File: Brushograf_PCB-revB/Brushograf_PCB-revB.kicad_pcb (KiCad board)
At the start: 2 copper layers, 200 x 75 mm, 75 parts, among them J1 Conn_01x05_Socket, J12 USB-C PD in, J13 Pendant, J2 Conn_01x05_Socket, J3 Conn_01x05_Socket, J8 SD_CARD_MICRO_AMPHENOL_114008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, SW1 ESP POWER, SW2 SW_Lever_1P2T_NKK_GW12LxH, U1 ULN2003A, U2 ULN2003A, U3 ULN2003A, U4 ESP32-DevKitC, U6 CH224K, U7 TPS54202, U8 TPS54202

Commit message: Rotate piezo pickup headers to be horizontal and mathematically center them
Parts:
- moved J_X_Pickup 3.81 mm to (126.2, 38.0), turned to 90 degrees
- moved J_Y_Pickup 3.81 mm to (186.2, 38.0), turned to 90 degrees
- moved J_Z_Pickup 3.81 mm to (66.2, 38.0), turned to 90 degrees
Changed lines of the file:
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@@
 		(locked yes)
 		(layer "F.Cu")
-		(at 130 38)
+		(at 126.19 38 90)
 		(descr "Through hole straight pin header, 1x04, 2.54mm pitch, single row")
 		(tags "Through hole pin header THT 1x04 2.54mm single row")
 		(property "Reference" "J_X_Pickup"
-			(at 0 -2.38 0)
+			(at 0 -2.38 90)
 			(layer "F.SilkS")
 			(effects
@@
 		)
 		(property "Value" "PinHeader_1x04_P2.54mm_Vertical"
-			(at 0 10 0)
+			(at 0 10 90)
 			(layer "F.Fab")
 			(effects
@@
 		)
 		(property "Datasheet" ""
-			(at 0 0 0)
+			(at 0 0 90)
 			(layer "F.Fab")
 			(hide yes)
@@
 		)
 		(property "Description" ""
-			(at 0 0 0)
+			(at 0 0 90)
 			(layer "F.Fab")
 			(hide yes)
@@
 		)
 		(property "KiLib_Generator" "connector/pin_header_socket"
-			(at 0 0 0)
+			(at 0 0 90)
 			(layer "F.SilkS")
 			(hide yes)
@@
 		)
 		(fp_line
-			(start -1.38 1.27)
-			(end -1.38 9)
+			(start 1.38 1.27)
+			(end 1.38 9)
 			(stroke
 				(width 0.12)
@@
 		)
 		(fp_line
-			(start -1.38 9)
-			(end 1.38 9)
+			(start -1.38 1.27)
+			(end -1.38 9)
 			(stroke
 				(width 0.12)
@@
 		)
 		(fp_line
-			(start 1.38 1.27)
+			(start -1.38 9)
 			(end 1.38 9)
 			(stroke
@@
 		)
 		(fp_line
-			(start -1.27 -0.635)
-			(end -0.635 -1.27)
+			(start 1.27 -1.27)
+			(end 1.27 8.89)
 			(stroke
 				(width 0.1)
@@
 		)
 		(fp_line
-			(start -1.27 8.89)
-			(end -1.27 -0.635)
+			(start -0.635 -1.27)
+			(end 1.27 -1.27)
 			(stroke
 				(width 0.1)
@@
 		)
 		(fp_line
-			(start -0.635 -1.27)
-			(end 1.27 -1.27)
+			(start -1.27 -0.635)
+			(end -0.635 -1.27)
 			(stroke
 				(width 0.1)
@@
 		)
 		(fp_line
-			(start 1.27 -1.27)
-			(end 1.27 8.89)
+			(start 1.27 8.89)
+			(end -1.27 8.89)
 			(stroke
 				(width 0.1)
@@
 		)
 		(fp_line
-			(start 1.27 8.89)
-			(end -1.27 8.89)
+			(start -1.27 8.89)
+			(end -1.27 -0.635)
 			(stroke
 				(width 0.1)
@@
 		)
 		(fp_text user "${REFERENCE}"
-			(at 0 3.81 90)
+			(at 0 3.81 180)
 			(layer "F.Fab")
 			(effects
@@
 		)
 		(pad "1" thru_hole rect
-			(at 0 0)
+			(at 0 0 90)
 			(size 1.7 1.7)
 			(drill 1)
@@
 		)
 		(pad "2" thru_hole circle
-			(at 0 2.54)
+			(at 0 2.54 90)
 			(size 1.7 1.7)
 			(drill 1)
@@
 		)
 		(pad "3" thru_hole circle
-			(at 0 5.08)
+			(at 0 5.08 90)
 			(size 1.7 1.7)
 			(drill 1)
@@
 		)
 		(pad "4" thru_hole circle
-			(at 0 7.62)
+			(at 0 7.62 90)
 			(size 1.7 1.7)
 			(drill 1)
@@
 		(locked yes)
 		(layer "F.Cu")
-		(at 190 38)
+		(at 186.19 38 90)
 		(descr "Through hole straight pin header, 1x04, 2.54mm pitch, single row")
 		(tags "Through hole pin header THT 1x04 2.54mm single row")
 		(property "Reference" "J_Y_Pickup"
-			(at 0 -2.38 0)
+			(at 0 -2.38 90)
 			(layer "F.SilkS")
 			(effects
@@
 		)
 		(property "Value" "PinHeader_1x04_P2.54mm_Vertical"
-			(at 0 10 0)
+			(at 0 10 90)
 			(layer "F.Fab")
 			(effects
@@
 		)
 		(property "Datasheet" ""
-			(at 0 0 0)
+			(at 0 0 90)
 			(layer "F.Fab")
 			(hide yes)
@@
 		)
 		(property "Description" ""
-			(at 0 0 0)
+			(at 0 0 90)
 			(layer "F.Fab")
 			(hide yes)
@@
 		)
 		(property "KiLib_Generator" "connector/pin_header_socket"
-			(at 0 0 0)
+			(at 0 0 90)
 			(layer "F.SilkS")
 			(hide yes)
@@
 		)
 		(fp_line
-			(start -1.38 1.27)
-			(end -1.38 9)
+			(start 1.38 1.27)
+			(end 1.38 9)
 			(stroke
 				(width 0.12)
@@
 		)
 		(fp_line
-			(start -1.38 9)
-			(end 1.38 9)
+			(start -1.38 1.27)
+			(end -1.38 9)
 			(stroke
 				(width 0.12)
@@
 		)
 		(fp_line
-			(start 1.38 1.27)
+			(start -1.38 9)
 			(end 1.38 9)
 			(stroke
@@
 		)
 		(fp_line
-			(start -1.27 -0.635)
-			(end -0.635 -1.27)
+			(start 1.27 -1.27)
+			(end 1.27 8.89)
 			(stroke
 				(width 0.1)
@@
 		)
 		(fp_line
-			(start -1.27 8.89)
-			(end -1.27 -0.635)
+			(start -0.635 -1.27)
+			(end 1.27 -1.27)
 			(stroke
 				(width 0.1)
@@
 		)
 		(fp_line
-			(start -0.635 -1.27)
-			(end 1.27 -1.27)
+			(start -1.27 -0.635)
+			(end -0.635 -1.27)
 			(stroke
 				(width 0.1)
@@
 		)
 		(fp_line
-			(start 1.27 -1.27)
-			(end 1.27 8.89)
+			(start 1.27 8.89)
+			(end -1.27 8.89)
 			(stroke
 				(width 0.1)
@@
 		)
 		(fp_line
-			(start 1.27 8.89)
-			(end -1.27 8.89)
+			(start -1.27 8.89)
+			(end -1.27 -0.635)
 			(stroke
 				(width 0.1)
@@
 		)
 		(fp_text user "${REFERENCE}"
-			(at 0 3.81 90)
+			(at 0 3.81 180)
 			(layer "F.Fab")
 			(effects
@@
 		)
 		(pad "1" thru_hole rect
-			(at 0 0)
+			(at 0 0 90)
 			(size 1.7 1.7)
 			(drill 1)
@@
 		)
 		(pad "2" thru_hole circle
-			(at 0 2.54)
+			(at 0 2.54 90)
 			(size 1.7 1.7)
 			(drill 1)
@@
 		)
 		(pad "3" thru_hole circle
-			(at 0 5.08)
+			(at 0 5.08 90)
 			(size 1.7 1.7)
 			(drill 1)
@@
 		)
 		(pad "4" thru_hole circle
-			(at 0 7.62)
+			(at 0 7.62 90)
 			(size 1.7 1.7)
 			(drill 1)
@@
 		(locked yes)
 		(layer "F.Cu")
-		(at 70 38)
+		(at 66.19 38 90)
 		(descr "Through hole straight pin header, 1x04, 2.54mm pitch, single row")
 		(tags "Through hole pin header THT 1x04 2.54mm single row")
 		(property "Reference" "J_Z_Pickup"
-			(at 0 -2.38 0)
+			(at 0 -2.38 90)
 			(layer "F.SilkS")
 			(effects
@@
 		)
 		(property "Value" "PinHeader_1x04_P2.54mm_Vertical"
-			(at 0 10 0)
+			(at 0 10 90)
 			(layer "F.Fab")
 			(effects
@@
 		)
 		(property "Datasheet" ""
-			(at 0 0 0)
+			(at 0 0 90)
 			(layer "F.Fab")
 			(hide yes)
@@
 		)
 		(property "Description" ""
-			(at 0 0 0)
+			(at 0 0 90)
 			(layer "F.Fab")
 			(hide yes)
@@
 		)
 		(property "KiLib_Generator" "connector/pin_header_socket"
-			(at 0 0 0)
+			(at 0 0 90)
 			(layer "F.SilkS")
 			(hide yes)
@@
 		)
 		(fp_line
-			(start -1.38 1.27)
-			(end -1.38 9)
+			(start 1.38 1.27)
+			(end 1.38 9)
 			(stroke
 				(width 0.12)
@@
 		)
 		(fp_line
-			(start -1.38 9)
-			(end 1.38 9)
+			(start -1.38 1.27)
+			(end -1.38 9)
 			(stroke
 				(width 0.12)
@@
 		)
 		(fp_line
-			(start 1.38 1.27)
+			(start -1.38 9)
 			(end 1.38 9)
 			(stroke
@@
 		)
 		(fp_line
-			(start -1.27 -0.635)
-			(end -0.635 -1.27)
+			(start 1.27 -1.27)
+			(end 1.27 8.89)
 			(stroke
 				(width 0.1)
@@
 		)
 		(fp_line
-			(start -1.27 8.89)
-			(end -1.27 -0.635)
+			(start -0.635 -1.27)
+			(end 1.27 -1.27)
 			(stroke
 				(width 0.1)
@@
 		)
 		(fp_line
-			(start -0.635 -1.27)
-			(end 1.27 -1.27)
+			(start -1.27 -0.635)
+			(end -0.635 -1.27)
 			(stroke
 				(width 0.1)
@@
 		)
 		(fp_line
-			(start 1.27 -1.27)
-			(end 1.27 8.89)
+			(start 1.27 8.89)
+			(end -1.27 8.89)
 			(stroke
 				(width 0.1)
@@
 		)
 		(fp_line
-			(start 1.27 8.89)
-			(end -1.27 8.89)
+			(start -1.27 8.89)
+			(end -1.27 -0.635)
 			(stroke
 				(width 0.1)
@@
 		)
 		(fp_text user "${REFERENCE}"
-			(at 0 3.81 90)
+			(at 0 3.81 180)
 			(layer "F.Fab")
 			(effects
@@
 		)
 		(pad "1" thru_hole rect
-			(at 0 0)
+			(at 0 0 90)
 			(size 1.7 1.7)
 			(drill 1)
@@
 		)
 		(pad "2" thru_hole circle
-			(at 0 2.54)
+			(at 0 2.54 90)
 			(size 1.7 1.7)
 			(drill 1)
@@
 		)
 		(pad "3" thru_hole circle
-			(at 0 5.08)
+			(at 0 5.08 90)
 			(size 1.7 1.7)
 			(drill 1)
@@
 		)
 		(pad "4" thru_hole circle
-			(at 0 7.62)
+			(at 0 7.62 90)
 			(size 1.7 1.7)
 			(drill 1)

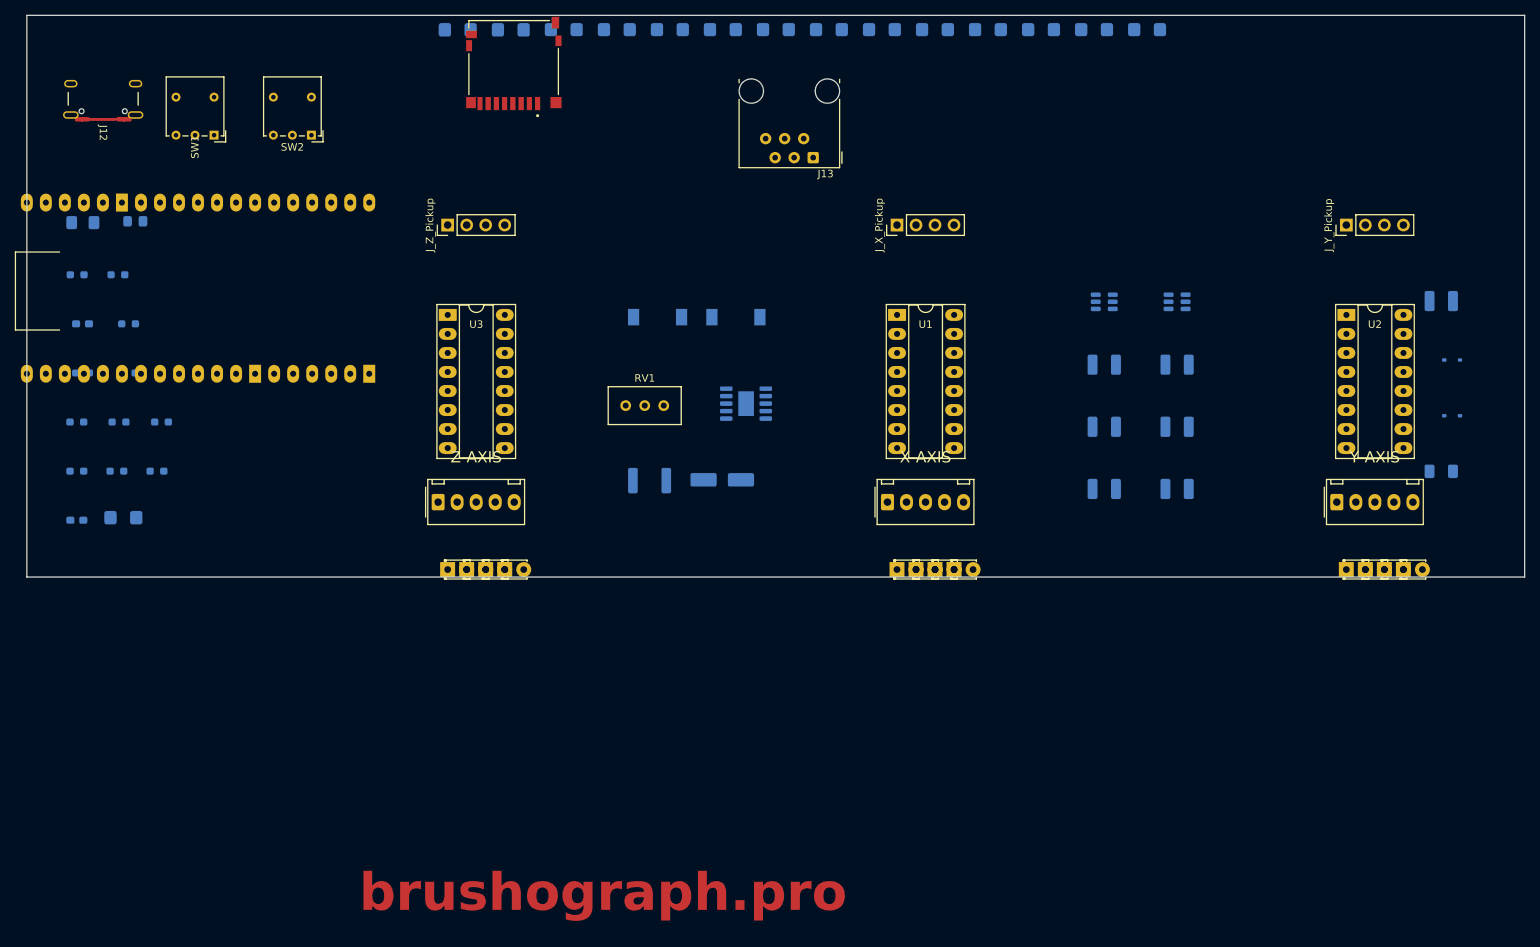
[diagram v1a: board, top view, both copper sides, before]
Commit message: Revert to tightly optimized 200x55 layout while preserving left-shifted motors and piezo headers
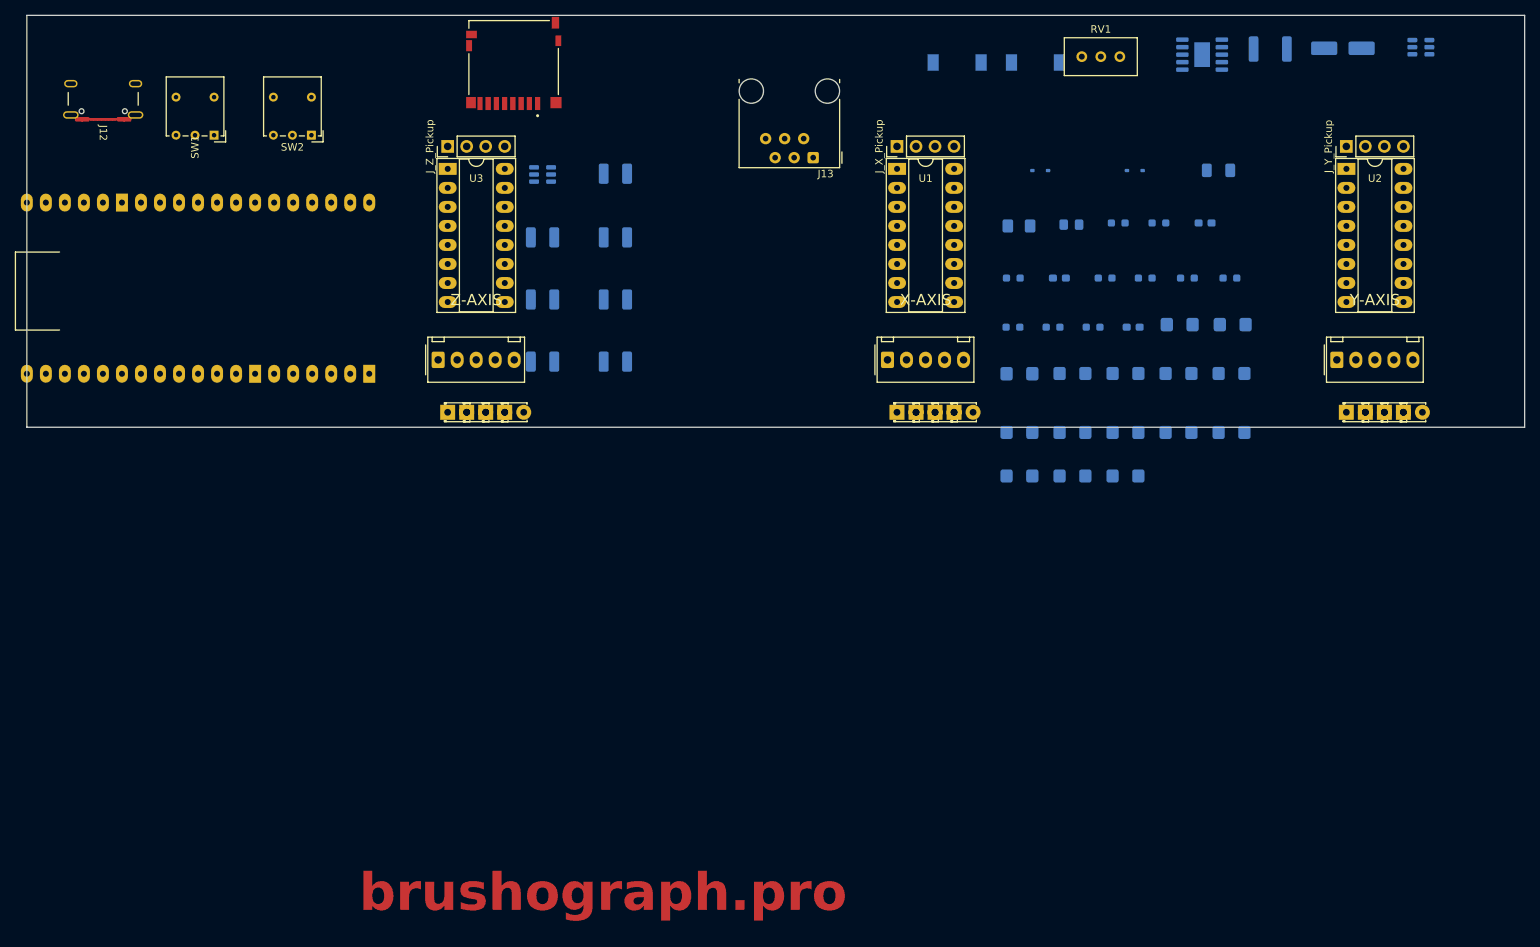
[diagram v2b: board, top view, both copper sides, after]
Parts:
- moved C16 150.5 mm to (167.3, 37.7)
- moved R26 143.9 mm to (165.0, 45.1)
- moved R31 143.9 mm to (159.3, 45.1)
- moved R23 143.9 mm to (170.6, 45.1)
- moved C9 143.4 mm to (157.7, 51.6)
- moved C3 143.4 mm to (163.9, 51.3)
- moved R27 139.2 mm to (155.7, 37.7)
- moved R24 139.2 mm to (161.2, 37.7)
- moved C12 131.1 mm to (147.9, 45.1)
- moved R28 131.1 mm to (154.0, 45.1)
- moved R29 126.5 mm to (141.7, 51.6)
- moved R25 126.5 mm to (152.4, 51.6)
- moved R30 126.5 mm to (147.0, 51.6)
- moved D17 125.0 mm to (149.5, 37.9)
- moved F2 125.0 mm to (142.5, 38.1)
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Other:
- board size 200 x 75 mm -> 200 x 55 mm

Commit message: Fix component spillage and add voltmeter header
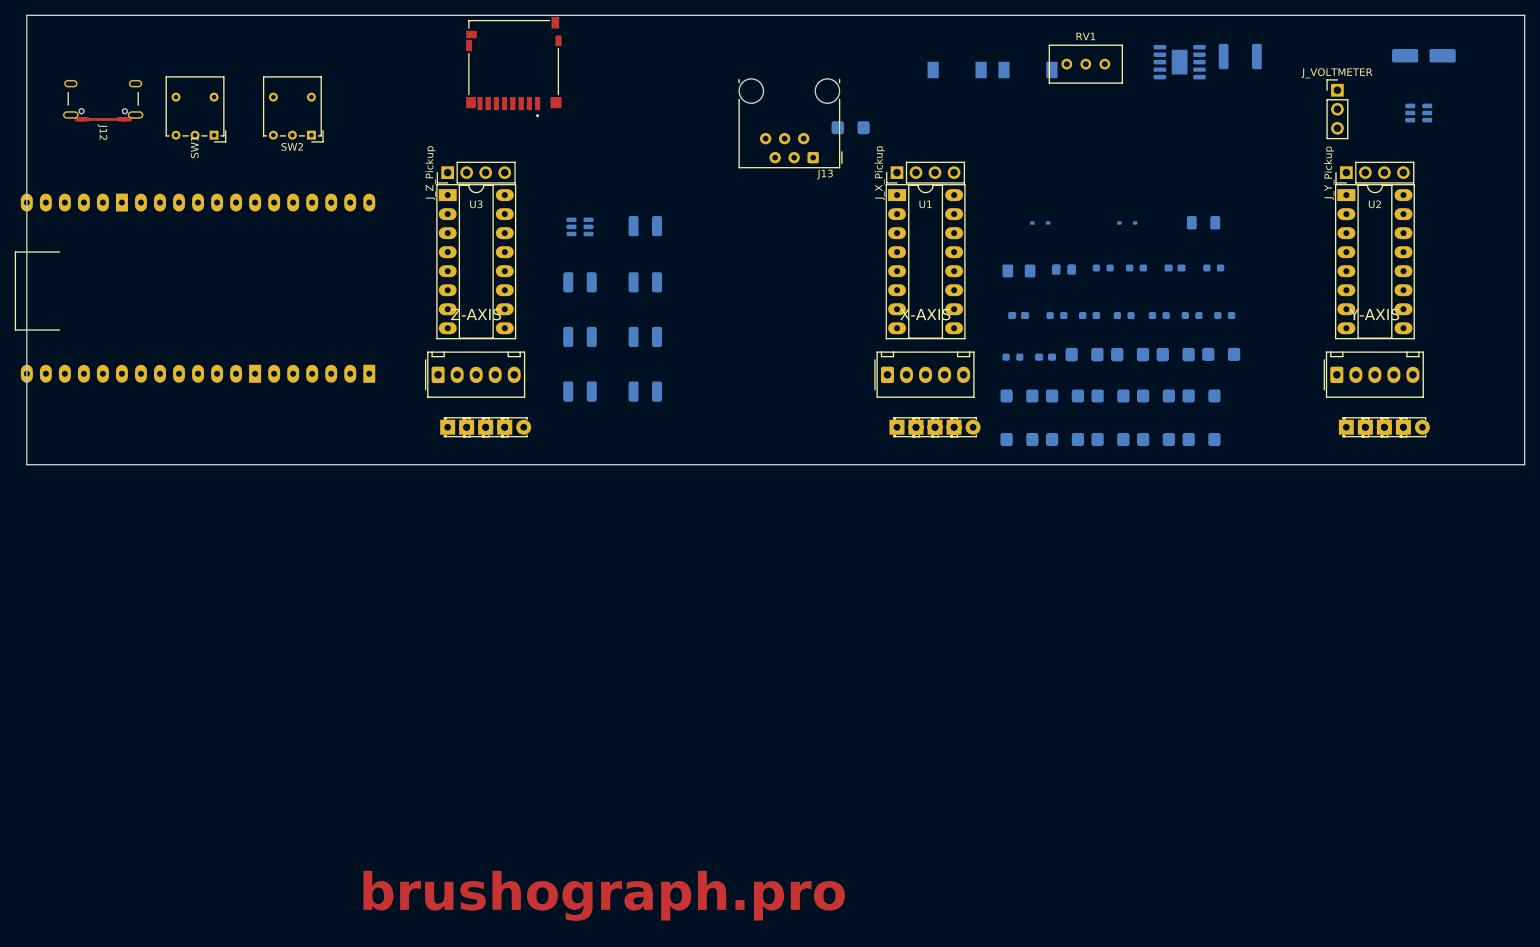
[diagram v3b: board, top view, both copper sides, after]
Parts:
- added J_VOLTMETER: PinHeader_1x03_P2.54mm_Vertical, PinHeader_1x03_P2.54mm_Vertical, F.Cu at (185.0, 20.0)
- moved R1 59.2 mm to (120.0, 25.0)
- moved R22 26.8 mm to (168.5, 43.7)
- moved R29 24.0 mm to (165.6, 50.1)
- moved R30 23.0 mm to (170.0, 50.1)
- moved C1 21.0 mm to (163.4, 55.3)
- moved R2 20.0 mm to (169.5, 55.3)
- moved R9 18.9 mm to (160.8, 60.8)
- moved R5 18.9 mm to (160.8, 66.6)
- moved R4 17.9 mm to (166.9, 60.8)
- moved R3 17.9 mm to (166.9, 66.6)
- moved R11 16.4 mm to (154.7, 60.8)
- moved R8 16.2 mm to (154.7, 66.6)
- moved R6 15.5 mm to (148.6, 60.8)
- moved R10 15.2 mm to (148.6, 66.6)
- moved R12 14.5 mm to (142.5, 60.8)
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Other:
- board size 200 x 55 mm -> 200 x 60 mm

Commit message: Auto-route densely packed 200x60 layout with piezo headers and voltmeter
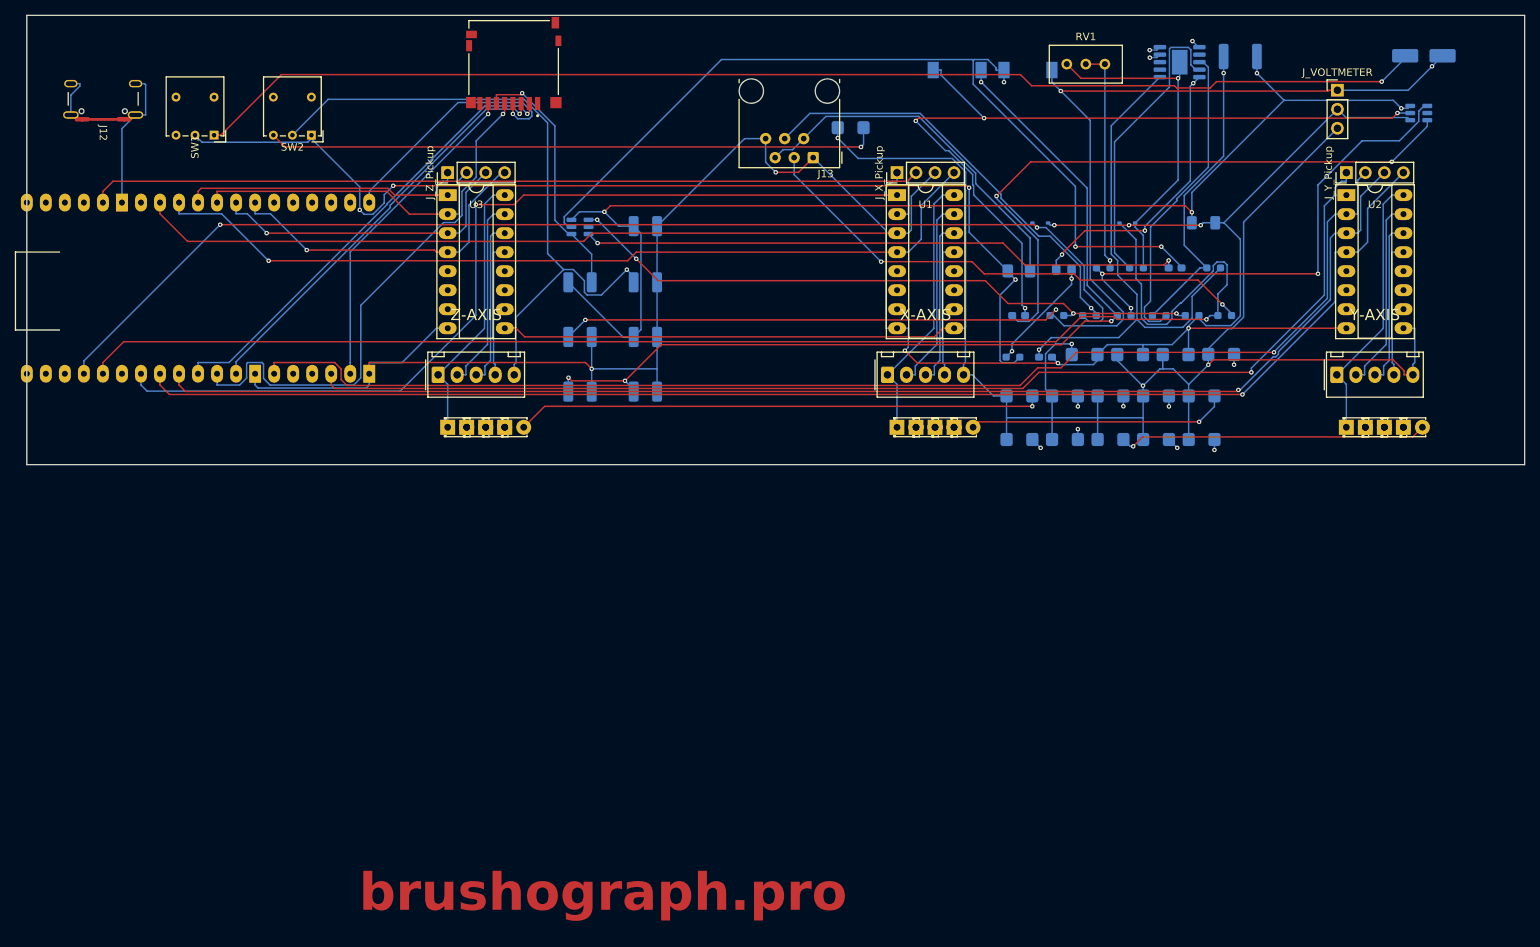
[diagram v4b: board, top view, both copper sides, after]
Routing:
- net GND: track 0.00 -> 417.5 mm, vias 0 -> 10
- net 5V: track 0.00 -> 363.8 mm, vias 0 -> 5
- net PEND_TX: track 0.00 -> 190.9 mm, vias 0 -> 1
- net IN4_U2: track 0.00 -> 186.9 mm, vias 0 -> 1
- net IN3_U2: track 0.00 -> 182.6 mm, vias 0 -> 1
- net IN2_U2: track 0.00 -> 169.8 mm, vias 0 -> 1
- net 5V_LOGIC: track 0.00 -> 168.5 mm, vias 0 -> 4
- net Net-(D14-K): track 0.00 -> 165.1 mm, vias 0 -> 1
- net VSUP: track 0.00 -> 162.3 mm, vias 0 -> 4
- net IN1_U2: track 0.00 -> 159.3 mm, vias 0 -> 1
- net PEND_RX: track 0.00 -> 157.2 mm, vias 0 -> 2
- net 5V_SYS: track 0.00 -> 142.3 mm, vias 0 -> 4
- net IN1_U1: track 0.00 -> 127.8 mm, vias 0 -> 1
- net MOTOR_V: track 0.00 -> 121.2 mm, vias 0 -> 4
- net IN2_U1: track 0.00 -> 118.6 mm
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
